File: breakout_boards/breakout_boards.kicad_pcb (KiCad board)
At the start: 2 copper layers, 49 x 21.4 mm, 53 parts, among them J1 USB_C_Receptacle_USB2.0, J2 USB_POWER_HEADER, J3 USB_POWER_HEADER_2, J4 ANALOG RGB HEADER, J5 ADDRESSIBLE RGB HEADER 1, J6 ADDRESSIBLE RGB HEADER 2, Q1 AO3400A, Q2 AO3400A, Q3 AO3400A, U1 CH340C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

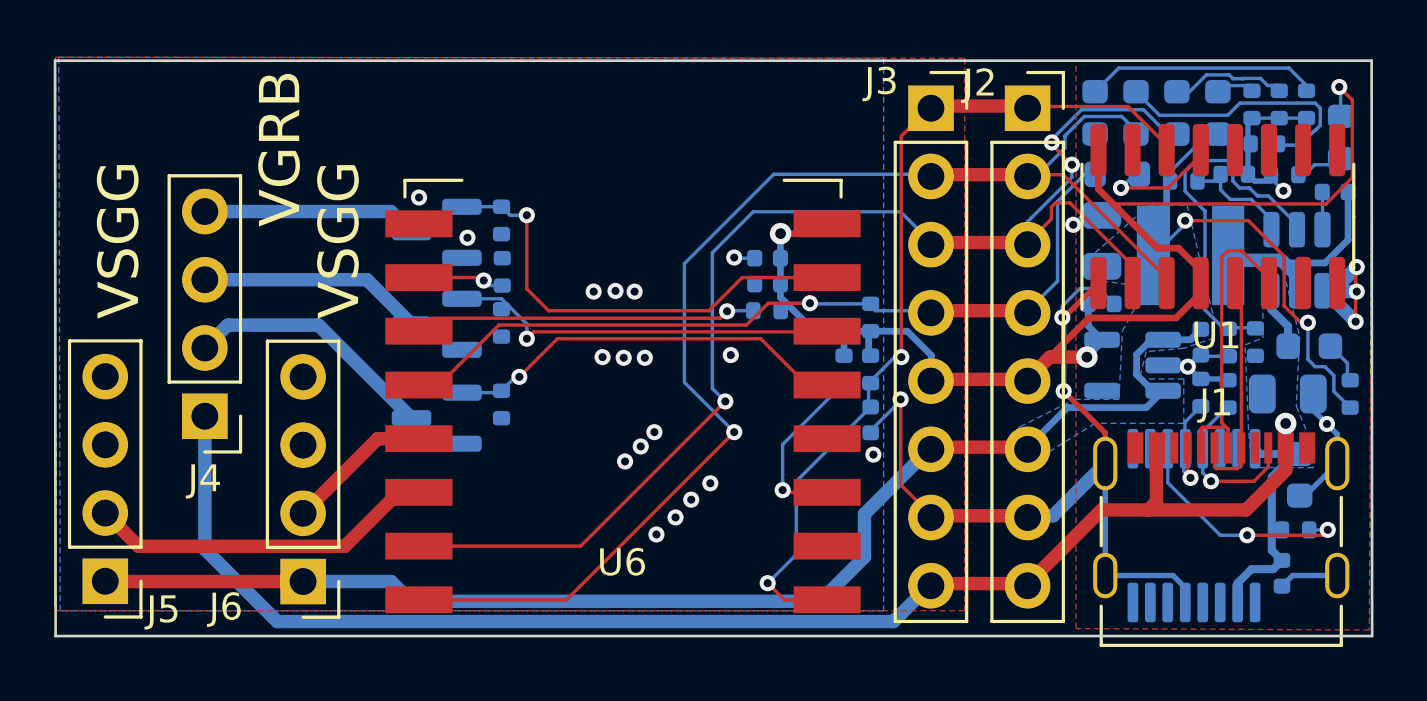
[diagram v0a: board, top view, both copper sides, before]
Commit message: V2.1
Increased current capacity, changed modules to be 30V tolerant
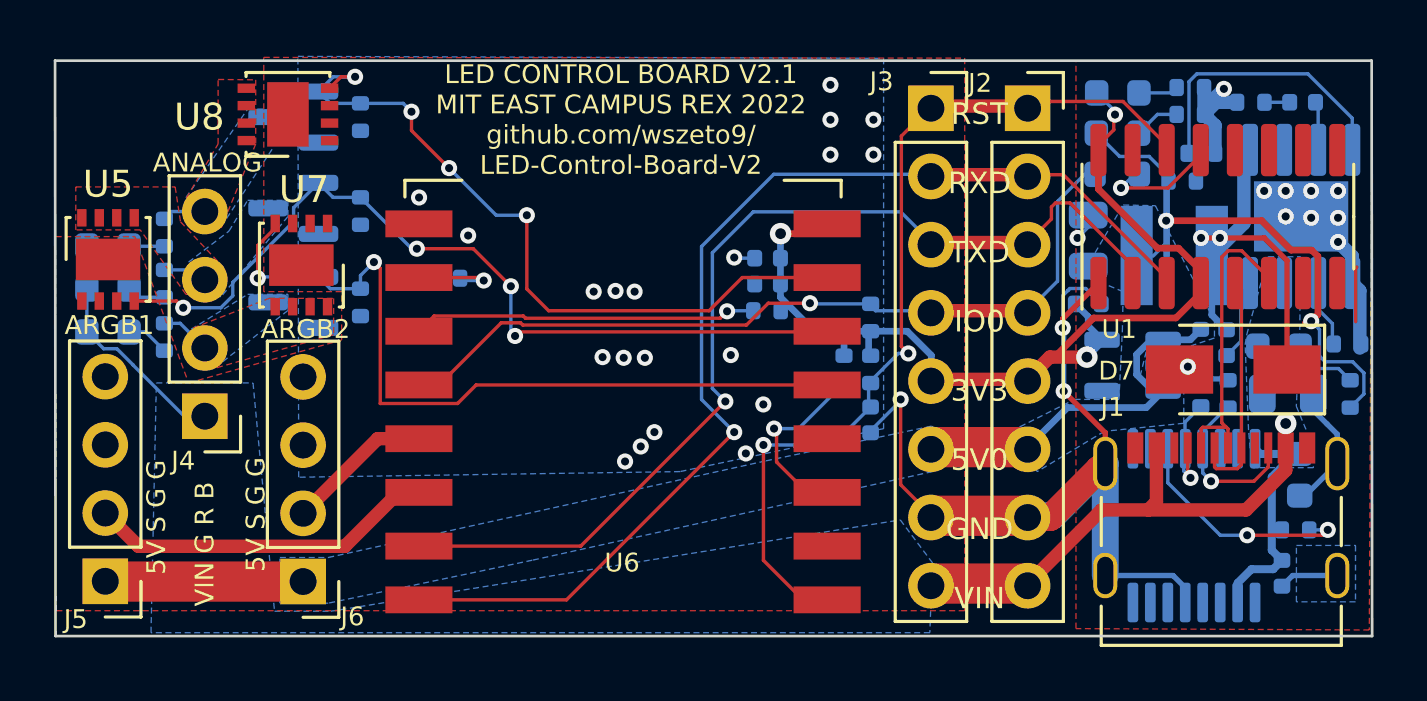
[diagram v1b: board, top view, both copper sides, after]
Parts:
- added C11: 150pF, Capacitor_SMD:C_0402_1005Metric, B.Cu at (168.5, 108.7)
- added D7: SS210, Diode_SMD:D_SMA, F.Cu at (165.9, 118.6)
- added U4: MP1584EN-LF-Z, Package_SO:SOIC-8-1EP_3.9x4.9mm_P1.27mm_EP2.62x3.51mm, B.Cu at (168.4, 112.9)
- added U7: SE3D080M, Package_DFN_QFN:DFN-8-1EP_3x3mm_P0.65mm_EP1.55x2.4mm, F.Cu at (131.2, 114.7)
- added U8: SE3D080M, Package_DFN_QFN:DFN-8-1EP_3x3mm_P0.65mm_EP1.55x2.4mm, F.Cu at (130.7, 109.1)
- C3: value 1uF -> 100nF
- D1: value LED -> LED_WHITE
- D2: value LED -> LED_RED
- D3: value LED -> LED_GREEN
- D4: value LED -> LED_B
- D5: value LED -> LED_G
- D6: value LED -> LED_R
- R16, R17, R18: value 1K -> 8.2k
- R6: value 100K -> 20k
- R7: value 19K -> 3.9k
- R8: value 12K -> 100K
- R9: value 10K -> 56k
- U5: value MT1470 -> SE3D080M; footprint Package_TO_SOT_SMD:TSOT-23-6 -> Package_DFN_QFN:DFN-8-1EP_3x3mm_P0.65mm_EP1.55x2.4mm; moved to F.Cu
- moved U5 44.3 mm to (124.0, 114.5)
- moved R16 42.8 mm to (126.1, 113.5), turned to 90 degrees
- moved R17 42.4 mm to (126.1, 117.4), turned to 90 degrees
- moved R18 41.3 mm to (126.1, 115.4), turned to 90 degrees
- moved D5 40.6 mm to (124.0, 117.2), turned to 180 degrees
- moved D6 38.8 mm to (124.0, 115.6), turned to 180 degrees
- moved D4 37.1 mm to (124.0, 114.0), turned to 180 degrees
- moved R8 8.93 mm to (166.6, 108.7), turned to 180 degrees
- moved D3 8.46 mm to (161.6, 108.3), turned to 180 degrees
- moved C3 6.91 mm to (165.7, 117.6), turned to 90 degrees
- moved Q2 6.87 mm to (130.9, 112.6)
- moved Q3 6.86 mm to (130.9, 116.1)
- moved Q1 6.85 mm to (130.9, 109.2)
- moved R11 6.70 mm to (133.4, 112.7)
- moved R10 6.51 mm to (133.4, 109.2)
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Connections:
- D4 pad 2: /GPIO0 -> VCC
- D5 pad 2: /TXD -> VCC
- D6 pad 2: /RXD -> VCC
- R16 pad 2: GND -> /B
- R17 pad 2: GND -> /G
- R18 pad 2: GND -> /R
- R8 pad 1: /5V_EN_H -> Net-(C11-Pad2)
- R8 pad 2: VCC -> GND
- R9 pad 1: GND -> Net-(R9-Pad1)
- R9 pad 2: /5V_EN_H -> GND
- U5 pad 2: /SW -> GND
- U5 pad 3: VCC -> GND
- U5 pad 4: /BUCK_FB -> /R_SIG
- U5 pad 5: /5V_EN_H -> /R
- U5 pad 6: Net-(C3-Pad1) -> /R
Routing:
- net VCC: track 65.3 -> 38.4 mm
- net +5V: track 67.4 -> 46.6 mm
- net /R_SIG: track 14.6 -> 31.9 mm, vias 1 -> 4
- net /G_SIG: track 15.1 -> 29.8 mm, vias 1 -> 2
- net /5V_EN_H: track 13.5 -> 0.00 mm
- net +3V3: track 52.1 -> 40.9 mm
- net /TXD: track 49.0 -> 38.6 mm, vias 3 -> 1
- net /B_SIG: track 17.3 -> 27.6 mm, vias 1 -> 4
- net Net-(D6-Pad1): track 10.1 -> 1.44 mm
- net /BUCK_FB: track 3.94 -> 11.9 mm
- net /G: track 9.48 -> 1.89 mm
- net Net-(D4-Pad1): track 8.51 -> 1.32 mm
- net /SW: track 8.47 -> 15.4 mm, vias 0 -> 2
- net /R: track 8.38 -> 1.66 mm
- net /B: track 8.02 -> 1.62 mm
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- added copper zone on B.Cu, net /B
- added copper zone on F.Cu, net /B
- added copper zone on B.Cu, net /G
- added copper zone on F.Cu, net /G
- added copper zone on B.Cu, net /R
- added copper zone on F.Cu, net /R
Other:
- board text added: "5V S G G"
- board text added: "ANALOG"
- board text added: "ARGB1"
- board text added: "ARGB2"
- board text added: "LED CONTROL BOARD V2.1 MIT EAST CAMPUS REX 2022 github.com/wszeto9/ LED-Control-Board-V2"
- board text added: "PINOUT IO4|ARGB2 IO5|ARGB1 IO12|R IO13|B IO14|G"
- board text added: "RST RXD TXD IO0 3V3 5V0 GND VIN"
- board text added: "TO CONTROL | POPULATE 5V ADDRESSIBLE | J1 12V ANALOG | J1 U2 D7 U4 24V ANALOG| INJECT ON VIN"
- board text added: "VIN G R B"
- board text removed: "LED CONTROL BOARD V2.0 MIT EAST CAMPUS REX 2022"
- board text removed: "VGRB"
- board text removed: "VSGG"
